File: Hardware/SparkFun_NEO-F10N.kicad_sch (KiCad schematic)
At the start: 49 parts, among them J1 USB_C_Receptacle, U1 TVS_ESD_USB, U2 AP2112K-3.3, U3 NEO-F10N, U8 CH340C

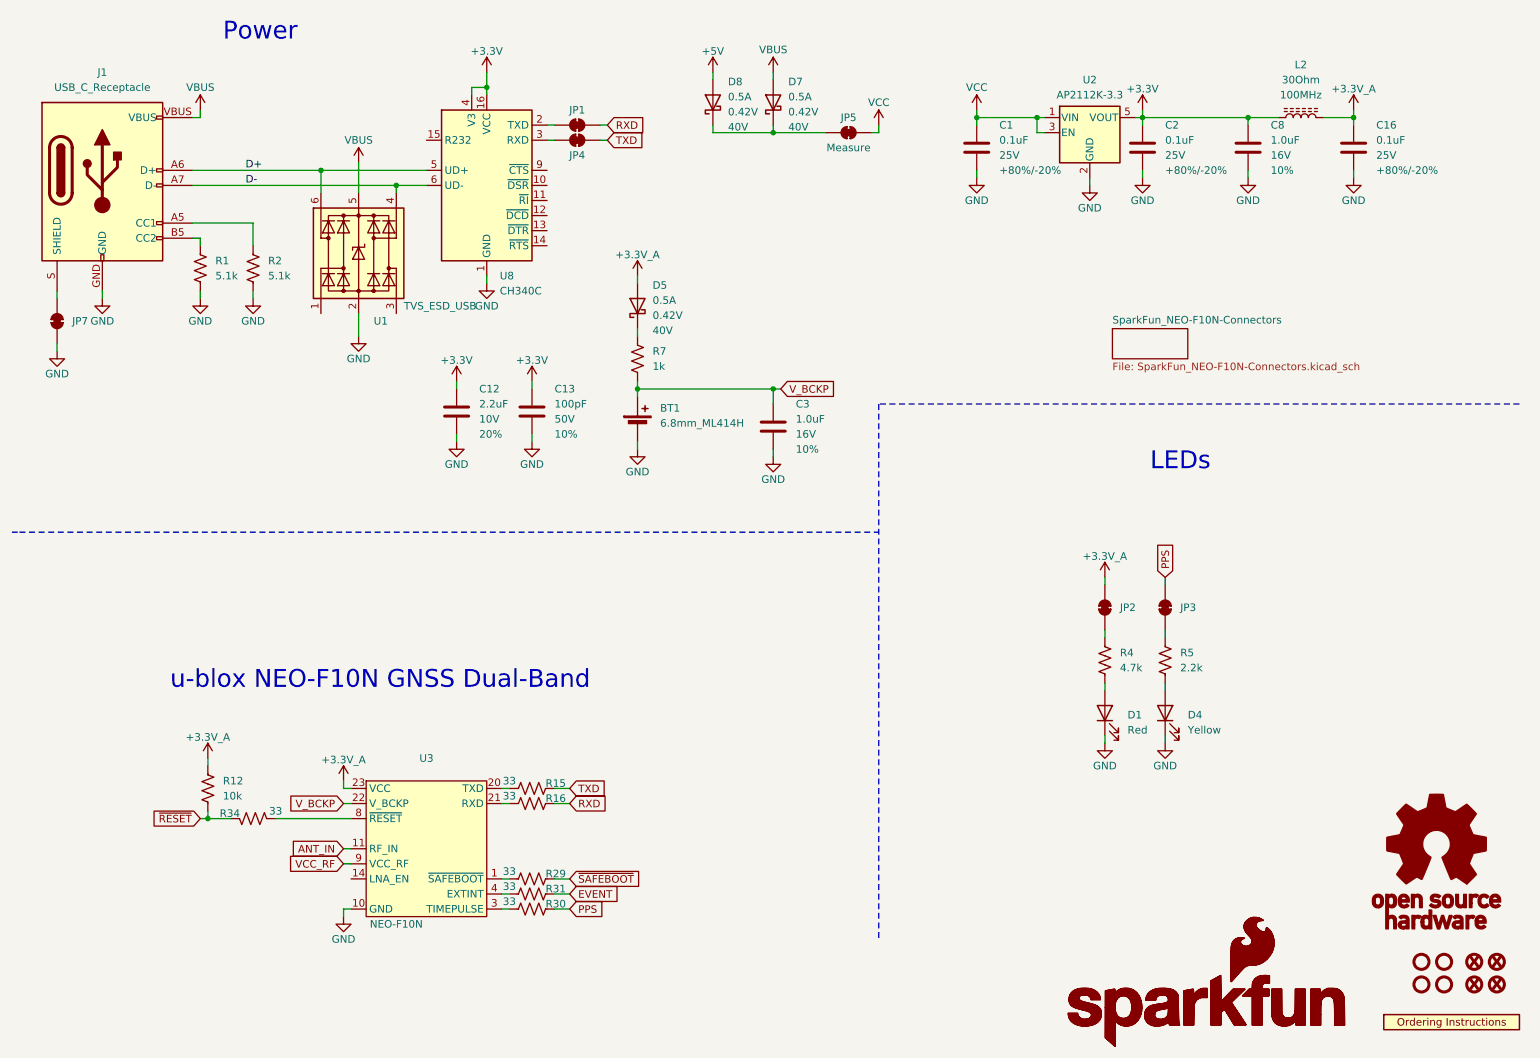
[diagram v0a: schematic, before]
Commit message: Update layout and panel files post design review.
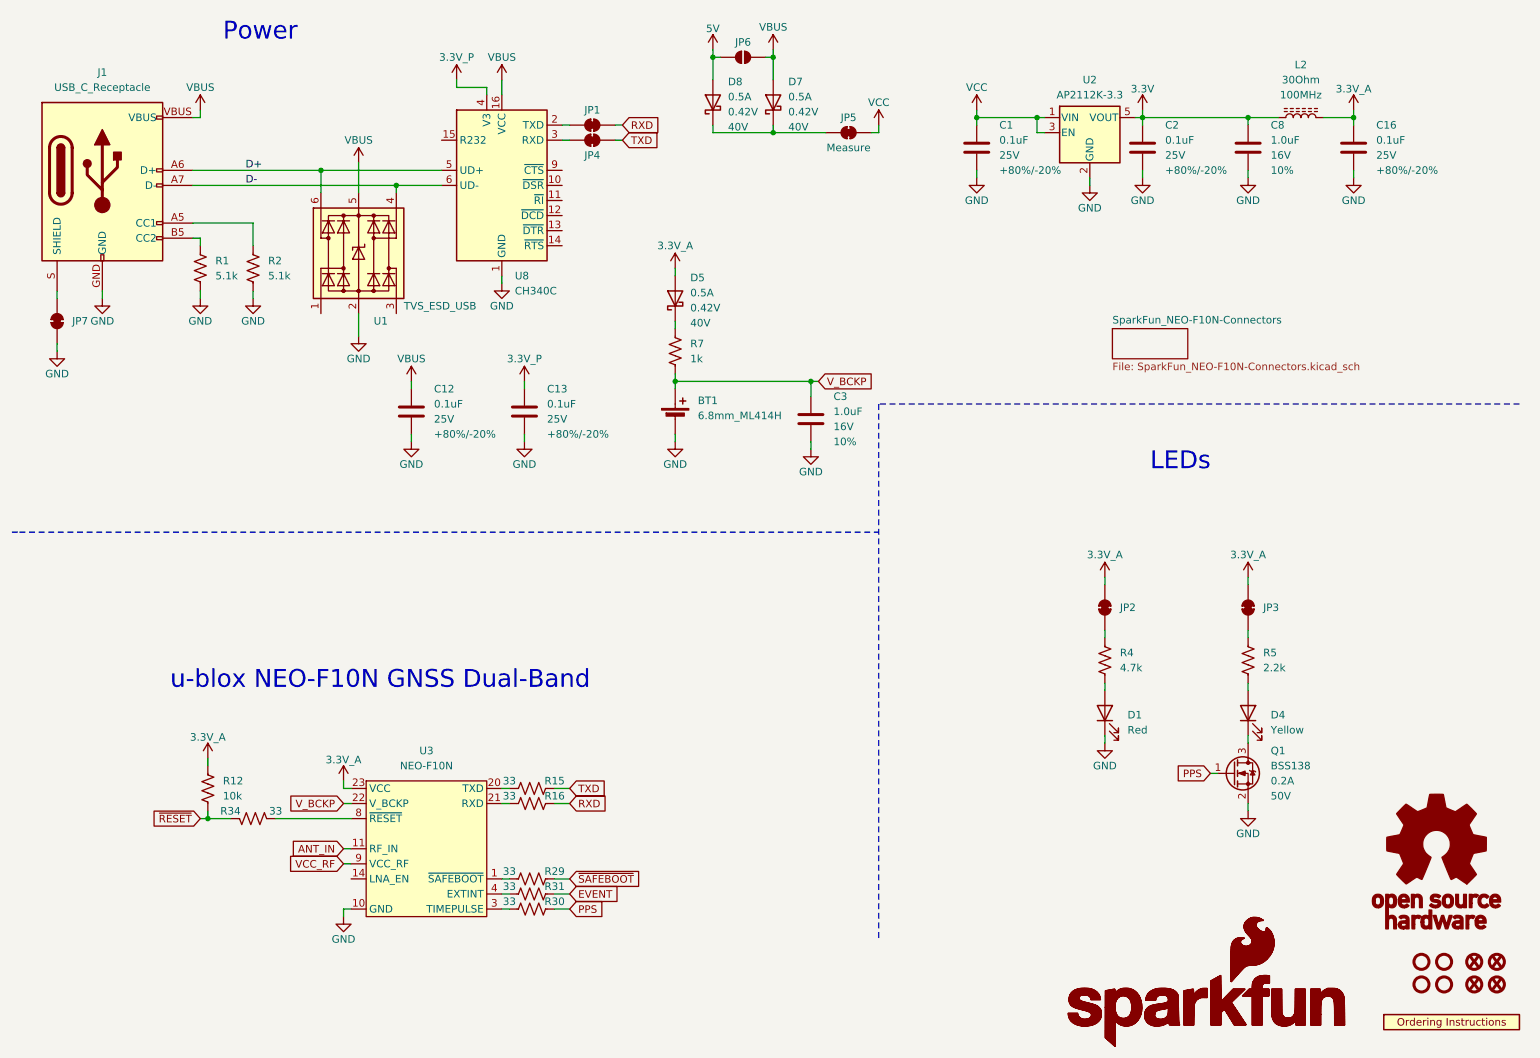
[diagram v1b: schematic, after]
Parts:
- added JP6: ~, SparkFun-Jumper:SMT-JUMPER_2_NO_SILK, symbol SparkFun-Jumper:SolderJumper_2_Open
- added Q1: BSS138, SparkFun-Semiconductor-Standard:SOT23-3, symbol SparkFun-DiscreteSemi:Q_NMOS_0.2A_50V
- C12: value 2.2uF -> 0.1uF; symbol SparkFun-Capacitor:2.2uF_0603_10V_20% -> SparkFun-Capacitor:0.1uF_0603_25V_20%; PROD_ID CAP-07888 -> CAP-00810; Tolerance 20% -> +80%/-20%; Voltage 10V -> 25V
- C13: value 100pF -> 0.1uF; symbol SparkFun-Capacitor:100pF_0603_50V_10% -> SparkFun-Capacitor:0.1uF_0603_25V_20%; PROD_ID CAP-07883 -> CAP-00810; Tolerance 10% -> +80%/-20%; Voltage 50V -> 25V
- FID1, FID2, FID3, FID4: value Fiducial_0.5 -> Fiducial_0.5mm; symbol SparkFun-Aesthetic:Fiducial_0.5 -> SparkFun-Aesthetic:Fiducial_0.5mm
- U2: Imax (none) -> 600mA; Iq (none) -> 55µA; VMax (none) -> 6V
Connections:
- net GND: now also Q1.2 (S); no longer D4.1 (K)
- net PPS: now also Q1.1 (G); no longer JP3.2 (B)
- net VBUS: now also C12.1, U8.16 (VCC), JP6.2 (B)
- net ~{RESET}: now also R34.1; no longer R34.2
- net at U3.8 (~{RESET}): now also R34.2; no longer R34.1
- net +3.3V renamed 3.3V
- net 3.3V: no longer C12.1, C13.1, U8.16 (VCC), U8.4 (V3)
- net +3.3V_A renamed 3.3V_A
- net 3.3V_A: now also JP3.2 (B)
- net +5V renamed 5V
- net 5V: now also JP6.1 (A)
- new net: D4.1 (K), Q1.3 (D)
- new net 3.3V_P: C13.1, U8.4 (V3)
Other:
- title: UM980 Triband GNSS Receiver Breakout -> NEO-F10N
- moved on the sheet: BT1, C12, C13, C3, D4, D5, JP1, JP3, JP4, R1, R12, R15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

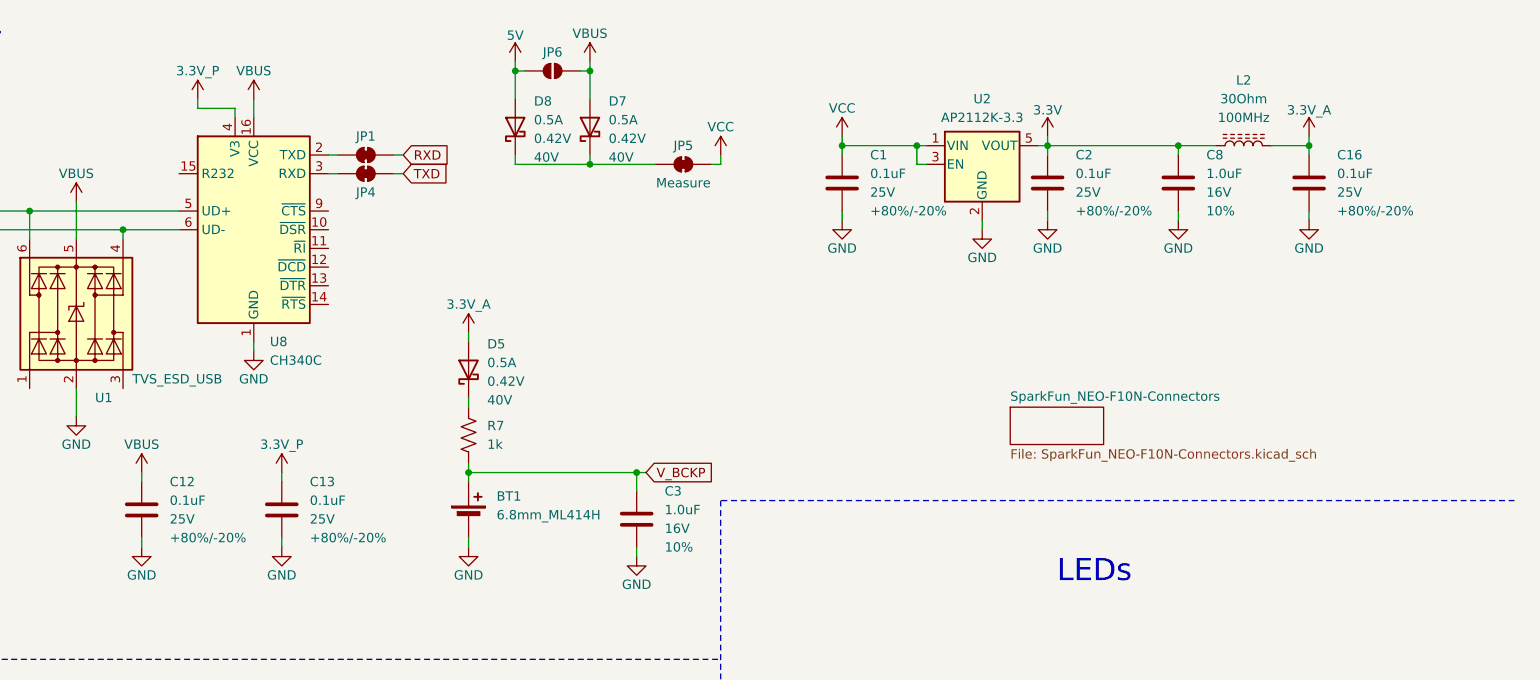
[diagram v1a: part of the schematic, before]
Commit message: Update 3D models
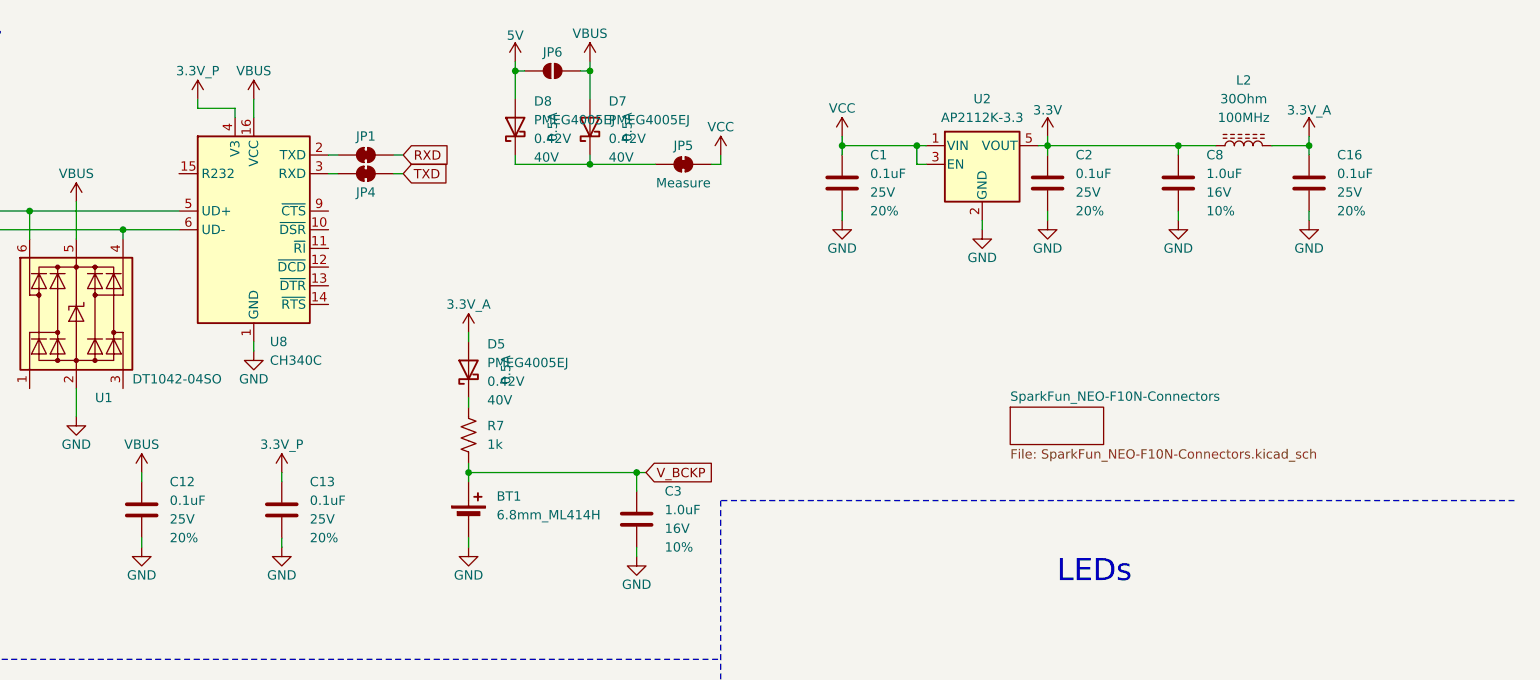
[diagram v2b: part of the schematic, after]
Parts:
- C1, C12, C13, C16, C2: Tolerance +80%/-20% -> 20%
- D1: footprint SparkFun-LED:LED_0603_1608Metric -> SparkFun-LED:LED_0603_1608Metric_Red
- D4: footprint SparkFun-LED:LED_0603_1608Metric -> SparkFun-LED:LED_0603_1608Metric_Yellow
- D5, D7, D8: value 0.5A -> PMEG4005EJ; IMax (none) -> 0.5A
- J1: footprint SparkFun-Connector:USB-C-16P -> SparkFun-Connector:USB-C_16
- JP1, JP2, JP3, JP4, JP7: footprint SparkFun-Jumper:SMT-JUMPER_2_NC_TRACE_SILK -> SparkFun-Jumper:Jumper_2_NC_Trace
- JP5: footprint SparkFun-Jumper:COMBO-JUMPER_2_NC_TRACE -> SparkFun-Jumper:Jumper_2_PTH_SMD_Combo-NC
- JP6: footprint SparkFun-Jumper:SMT-JUMPER_2_NO_SILK -> SparkFun-Jumper:Jumper_2_NO
- ST1, ST2, ST3, ST4: value Stand_off -> Standoff; footprint SparkFun-Hardware:STAND-OFF -> SparkFun-Hardware:Standoff; symbol SparkFun-Hardware:Stand_off -> SparkFun-Hardware:Standoff
- U1: value TVS_ESD_USB -> DT1042-04SO
- U7: footprint SparkFun-Aesthetic:ORDERING_INSTRUCTIONS -> SparkFun-Aesthetic:Ordering_Instructions
- U8: footprint SparkFun-Semiconductor-Standard:SO16 -> SparkFun-Semiconductor-Standard:SO-16
